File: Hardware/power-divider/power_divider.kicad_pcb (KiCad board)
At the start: 2 copper layers, 18 parts, among them J1 Conn_Coaxial_Power, J2 Conn_Coaxial_Power, J3 Conn_Coaxial_Power

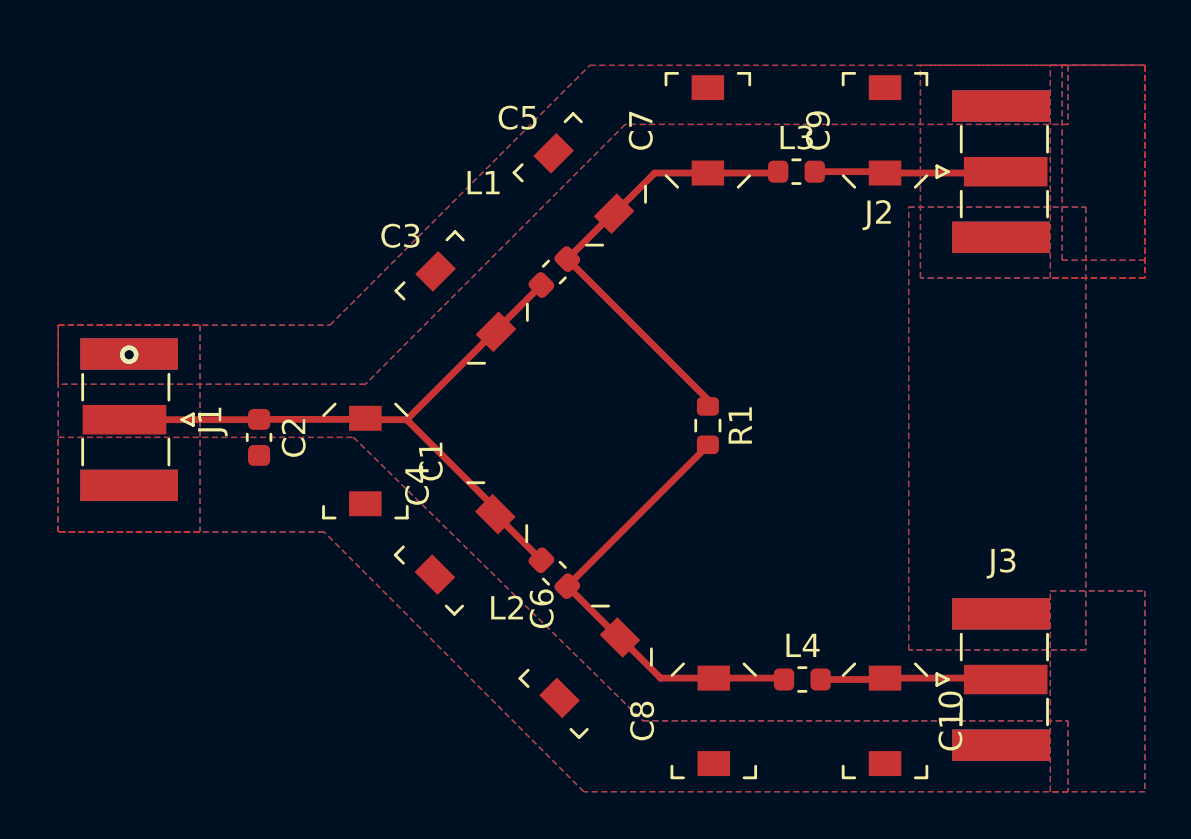
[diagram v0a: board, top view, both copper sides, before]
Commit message: Fixed zones, added edgecuts and vias
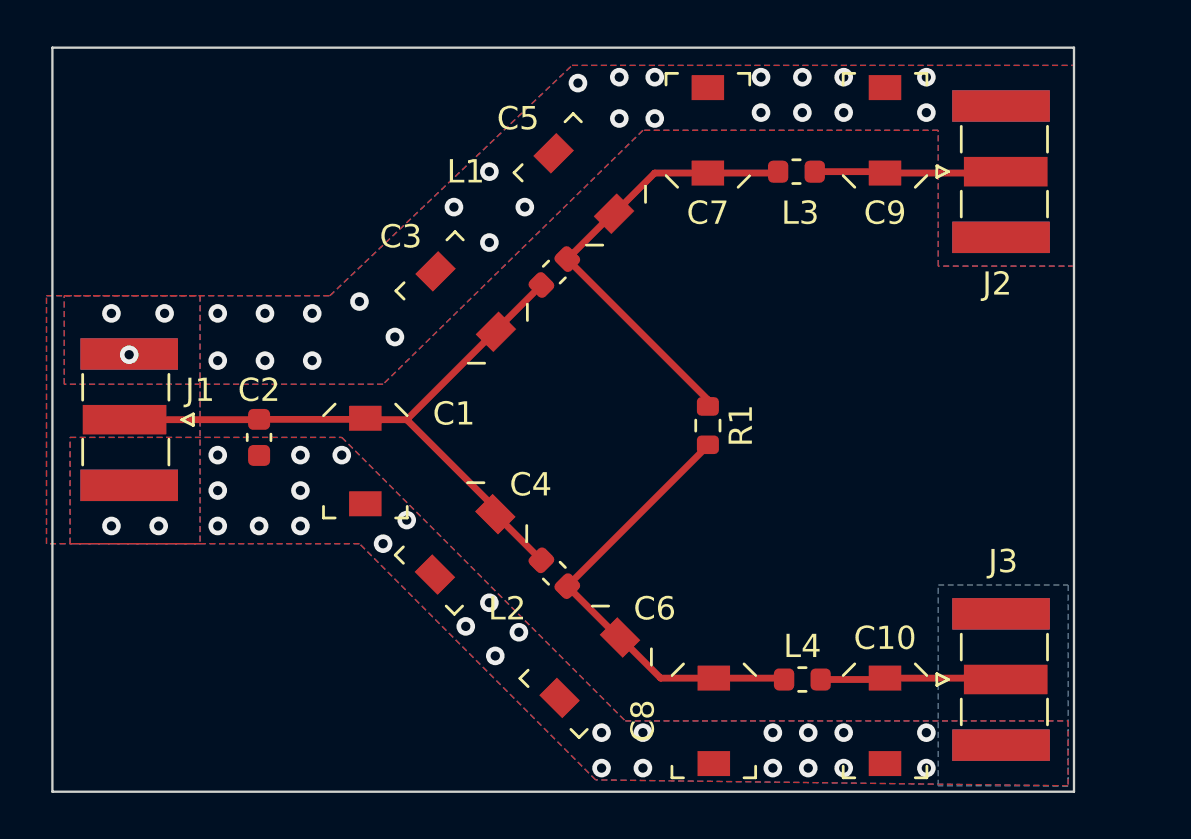
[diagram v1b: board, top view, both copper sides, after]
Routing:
- net GND: track 0.48 -> 0.00 mm, vias 1 -> 56
- removed copper zone on B.Cu, net (none)
- removed copper zone on F.Cu, net (none)
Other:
- board outline added: 43.9 x 32 mm
